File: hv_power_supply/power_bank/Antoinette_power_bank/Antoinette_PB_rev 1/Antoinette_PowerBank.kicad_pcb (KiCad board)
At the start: 2 copper layers, 30.5 x 48.3 mm, 51 parts, among them J1 NanoFit_RA_TH_02, J2 USB-Micro-1981568-1, J3 NanoFit_RA_TH_02, J4 USB-A-S-X-X-SM2, J5 NanoFit_RA_TH_02, Q1 SSM3K333R, U2 MCP73871T-2CCI_ML, U3 TPS61090RSAR

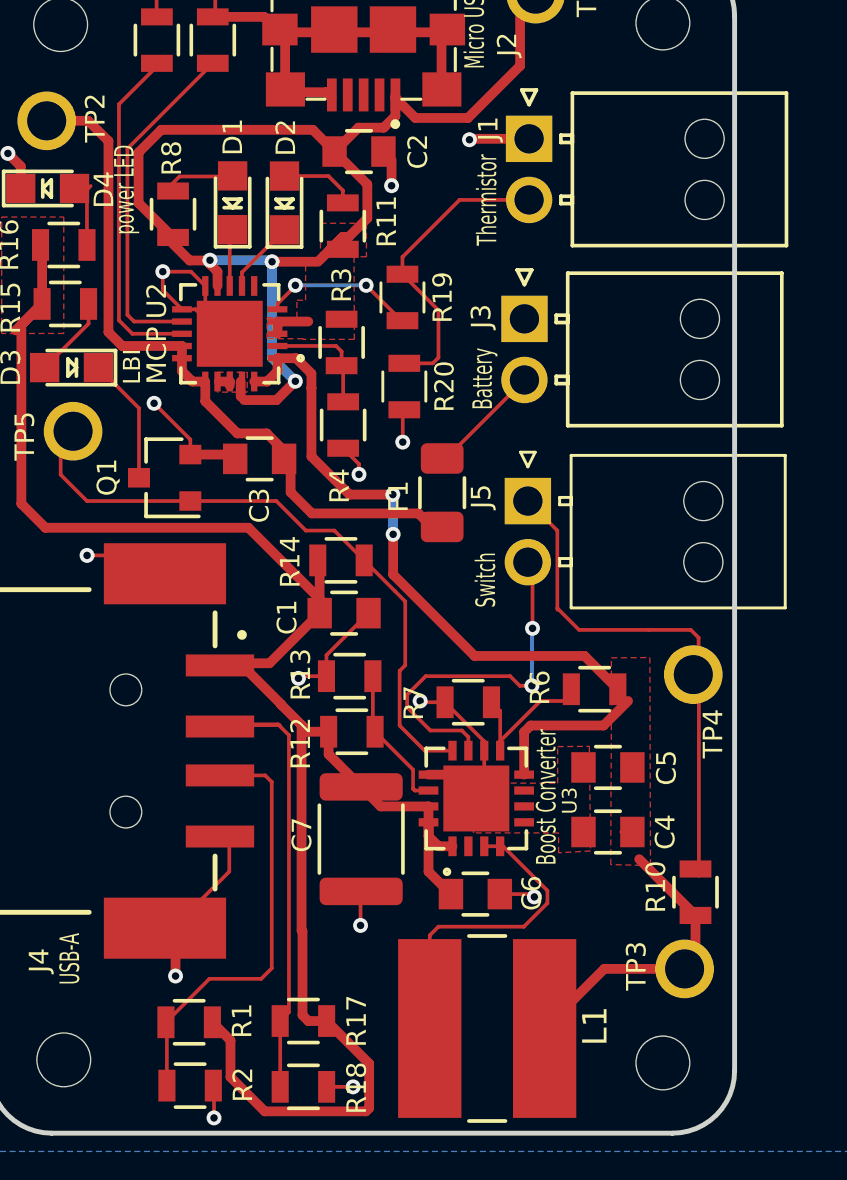
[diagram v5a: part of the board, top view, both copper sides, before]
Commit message: Modify PCB layout.
Create shorter vias, move trace through test point so current doesn't go through.
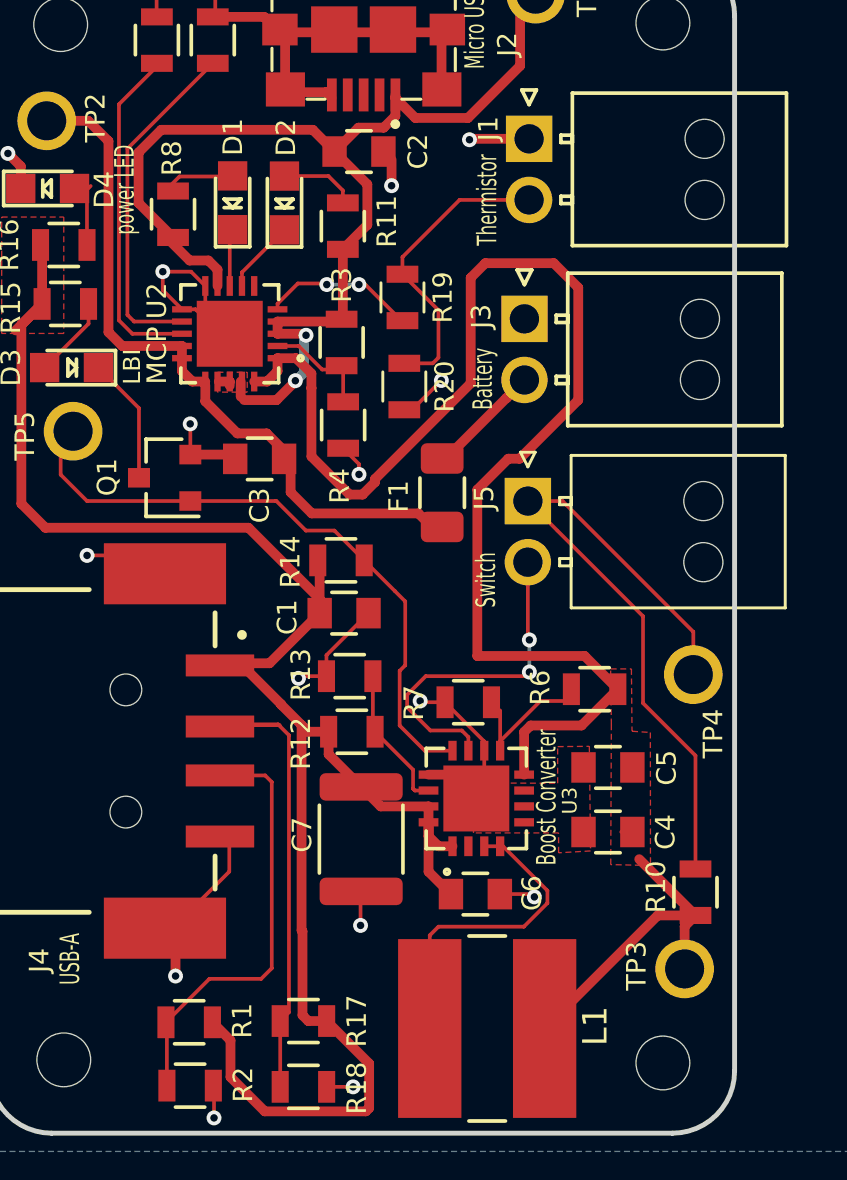
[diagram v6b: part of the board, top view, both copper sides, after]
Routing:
- net +BATT: track 43.5 -> 69.4 mm, vias 2 -> 0
- net Net-(J5-Pad1): track 21.6 -> 28.6 mm
- net VBUS: track 51.6 -> 47.7 mm, vias 3 -> 2
- net GND: track 68.6 -> 67.9 mm
